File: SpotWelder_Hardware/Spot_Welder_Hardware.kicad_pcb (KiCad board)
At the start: 2 copper layers, 263.7 x 182.9 mm, 158 parts, among them J1 Mini USB, J2 Conn_01x03_Male, Q1 Q_NMOS_GSD, Q10 Q_NMOS_GDS, Q11 Q_NMOS_GDS, Q12 Q_NMOS_GDS, Q13 Q_NMOS_GDS, Q2 MBT3904, Q3 Q_NMOS_GDS, Q4 Q_NMOS_GDS, Q5 Q_NMOS_GDS, Q6 Q_NMOS_GDS, Q7 Q_NMOS_GDS, Q8 Q_NMOS_GDS, Q9 Q_NMOS_GDS, SW1 SW_Push, SW2 SW_SPDT, SW3 Lead Voltage Trigger, SW4 SW_Push, U1 OKI, U2 ATMEGA328P, U3 FAN3122TMXCT-ND, U4 FT232RL, U5 FAN3122TMXCT-ND, Y1 Crystal

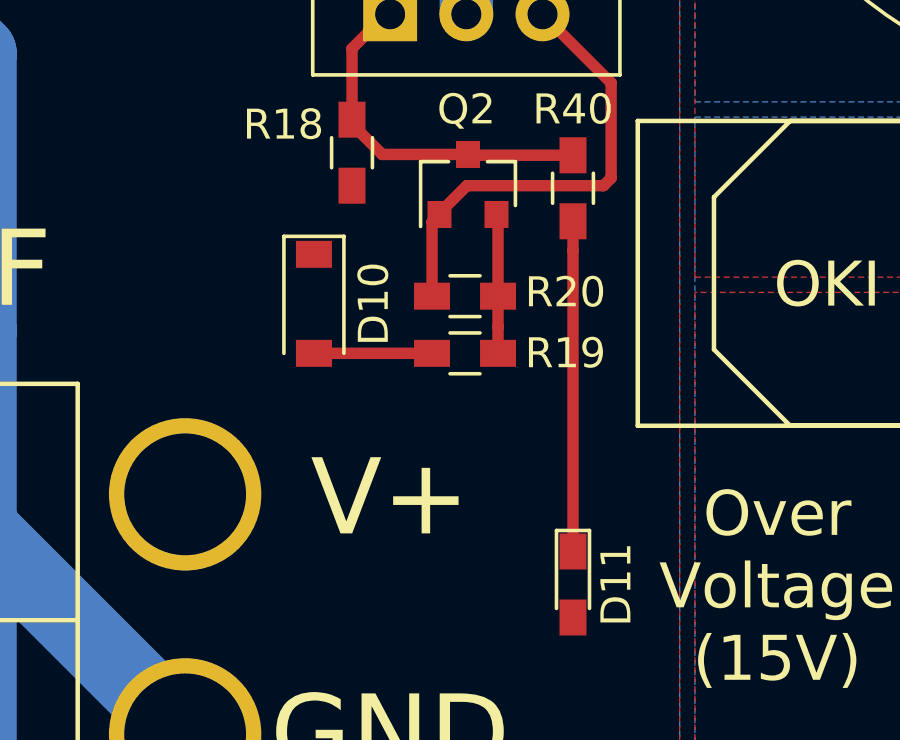
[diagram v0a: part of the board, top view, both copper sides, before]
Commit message: Cleaned repo structure and updated library mappings
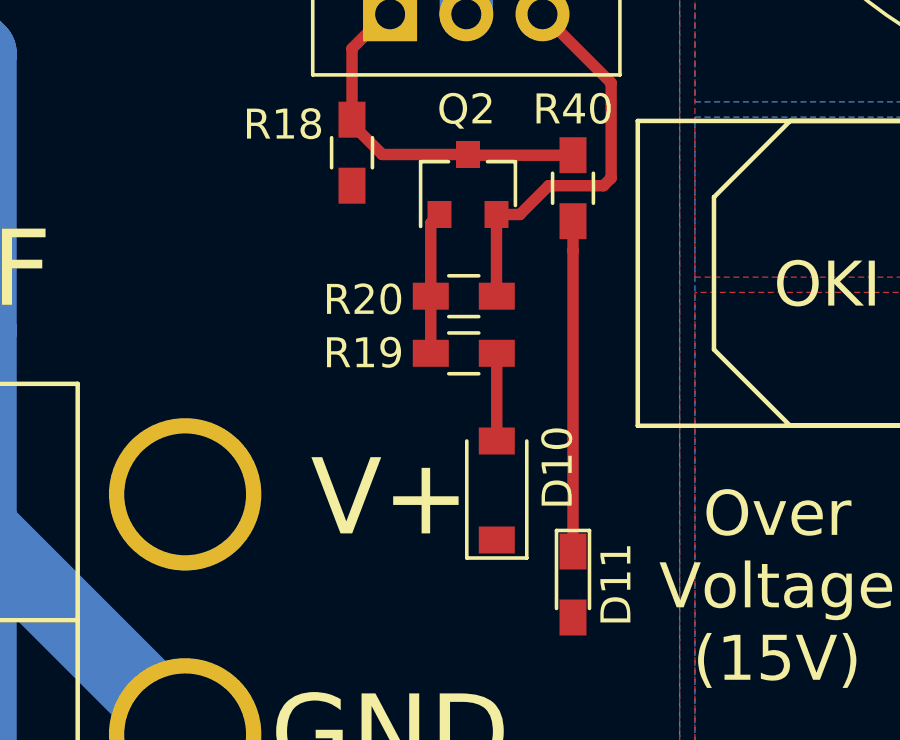
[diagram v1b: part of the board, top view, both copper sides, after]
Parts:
- moved D10 8.71 mm to (47.8, 152.4), turned to 90 degrees
- turned R19 to 0 degrees
- turned R20 to 0 degrees
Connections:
- J1 pad 4: (no net) -> Net-(J1-Pad4)
- Q2 pad 1: Power_GND -> Net-(Q2-Pad1)
- Q2 pad 2: Net-(Q2-Pad2) -> Power_GND
- R19 pad 1: Net-(Q2-Pad2) -> Net-(Q2-Pad1)
- R20 pad 1: Net-(Q2-Pad2) -> Net-(Q2-Pad1)
- U2 pad 14: (no net) -> Net-(U2-Pad14)
- U2 pad 19: (no net) -> Net-(U2-Pad19)
- U2 pad 25: (no net) -> Net-(U2-Pad25)
- U2 pad 26: (no net) -> Net-(U2-Pad26)
- U2 pad 27: (no net) -> Net-(U2-Pad27)
- U2 pad 28: (no net) -> Net-(U2-Pad28)
- U2 pad 4: (no net) -> Net-(U2-Pad4)
- U2 pad 5: (no net) -> Net-(U2-Pad5)
- U4 pad 10: (no net) -> Net-(U4-Pad10)
- U4 pad 11: (no net) -> Net-(U4-Pad11)
- U4 pad 12: (no net) -> Net-(U4-Pad12)
- U4 pad 13: (no net) -> Net-(U4-Pad13)
- U4 pad 14: (no net) -> Net-(U4-Pad14)
- U4 pad 24: (no net) -> Net-(U4-Pad24)
- U4 pad 27: (no net) -> Net-(U4-Pad27)
- U4 pad 28: (no net) -> Net-(U4-Pad28)
- U4 pad 3: (no net) -> Net-(U4-Pad3)
- U4 pad 6: (no net) -> Net-(U4-Pad6)
- U4 pad 8: (no net) -> Net-(U4-Pad8)
- U4 pad 9: (no net) -> Net-(U4-Pad9)
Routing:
- net Net-(Q2-Pad1): track 0.00 -> 4.75 mm
- net Net-(Q2-Pad2): track 4.65 -> 0.00 mm
- net Power_GND: track 15.6 -> 13.5 mm
- net Net-(D10-Pad2): track 4.11 -> 2.92 mm

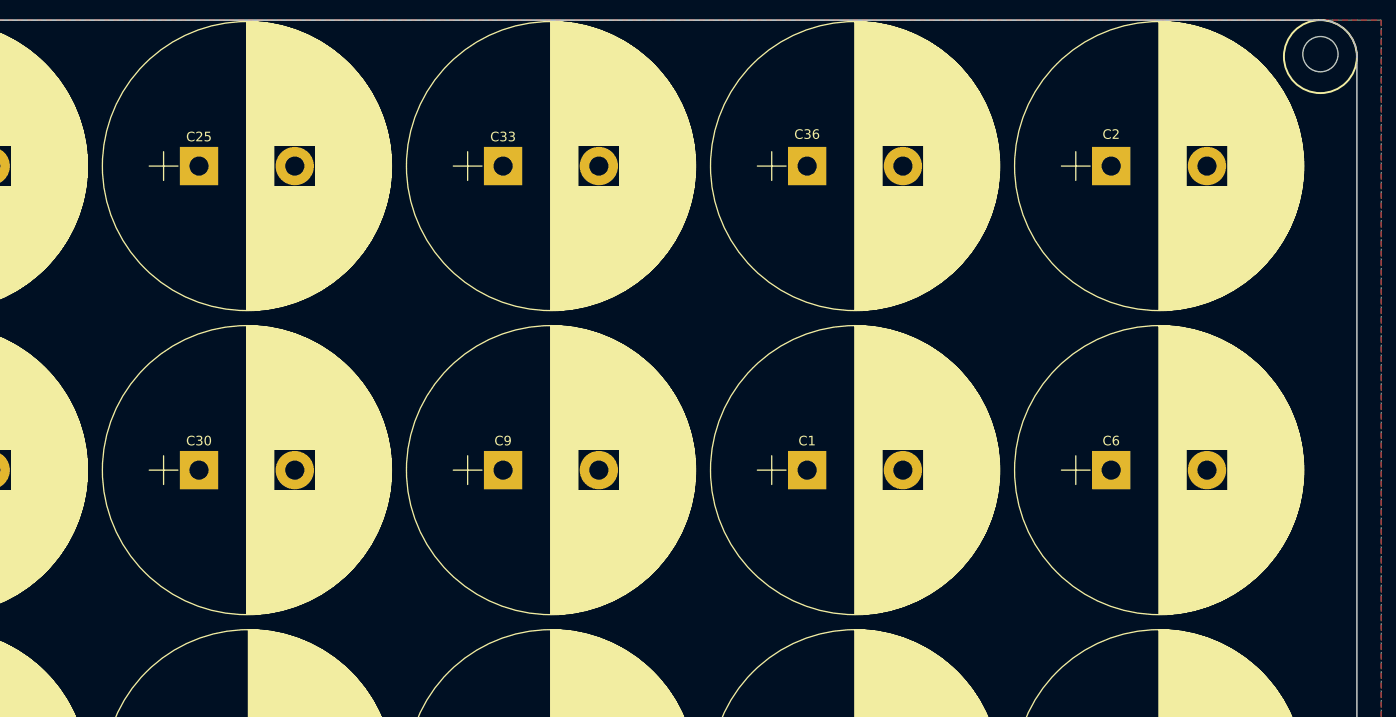
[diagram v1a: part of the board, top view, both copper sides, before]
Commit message: Added center support hole
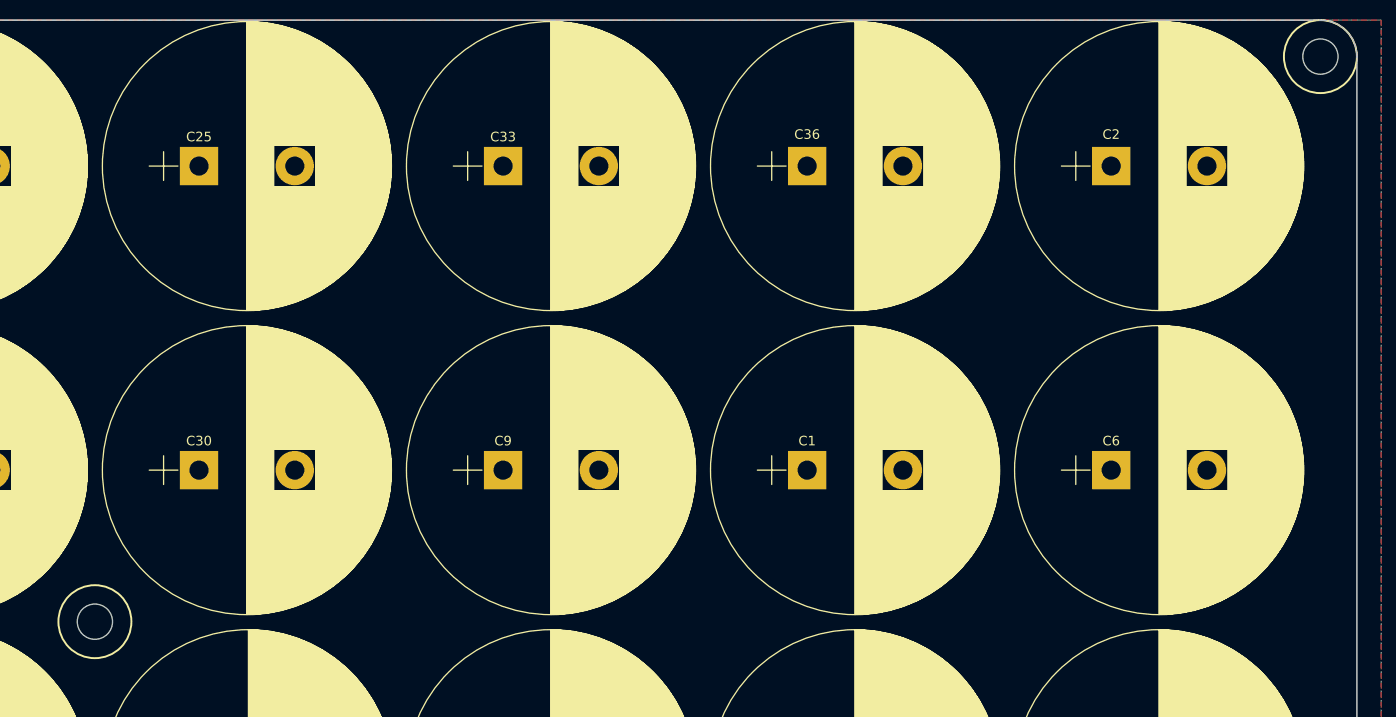
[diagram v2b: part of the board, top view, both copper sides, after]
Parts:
- added REF**: 6-32 Screw Hole, Project Library:6-32 Screw Hole, F.Cu at (139.5, 83.1)
- D10: value 15V -> 14V
- moved REF** 0.25 mm to (276.6, 17.5)
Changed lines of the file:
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@@
   (general
     (thickness 1.6)
-    (drawings 42)
+    (drawings 43)
     (tracks 595)
     (zones 0)
-    (modules 158)
+    (modules 159)
     (nets 95)
   )
@@
   )
   (module "Project Library:6-32 Screw Hole" (layer F.Cu)
+    (at 139.4968 83.1342 90)
+    (fp_text reference REF** (at 0 0.5 90) (layer F.SilkS) hide
+      (effects (font (size 1 1) (thickness 0.15)))
+    )
+    (fp_text value "6-32 Screw Hole" (at 0 -0.5 90) (layer F.Fab)
+      (effects (font (size 1 1) (thickness 0.15)))
+    )
+    (pad "" np_thru_hole circle (at 6.604 9.144 90) (size 3.683 3.683) (drill 3.683) (layers *.Cu *.Mask))
+  )
+  (module "Project Library:6-32 Screw Hole" (layer F.Cu)
     (at 274.574 192.786 180)
     (fp_text reference REF** (at 0 0.5 180) (layer F.SilkS) hide
@@
   )
   (module "Project Library:6-32 Screw Hole" (layer F.Cu)
-    (at 276.606 17.272 270)
+    (at 276.606 17.526 270)
     (fp_text reference REF** (at 0 0.5 270) (layer F.SilkS) hide
       (effects (font (size 1 1) (thickness 0.15)))
@@
       (effects (font (size 1 1) (thickness 0.15)))
     )
-    (fp_text value 15V (at 0 2.1 90) (layer F.Fab)
+    (fp_text value 14V (at 0 2.1 90) (layer F.Fab)
       (effects (font (size 1 1) (thickness 0.15)))
     )
@@
       (xy -6.395956 -0.780515) (xy -6.39578 -0.780671) (xy -6.278558 -0.884008) (xy -6.152213 -0.877709)) (layer F.SilkS) (width 0.01))
   )
+  (gr_circle (center 148.6408 76.5302) (end 152.4508 76.5302) (layer F.SilkS) (width 0.2))
   (gr_circle (center 276.606 192.786) (end 280.416 192.786) (layer F.SilkS) (width 0.2))
   (gr_arc (start 276.606 192.786) (end 276.606 196.596) (angle -90) (layer Edge.Cuts) (width 0.15))

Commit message: Updated version number
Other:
- board text added: "Spot Welder, Rev 3 Mars Rover Design Team, 2020 Missouri S&T Andrew Van Horn With help from Robert Ruark"
- board text removed: "Spot Welder, Rev 2 Mars Rover Design Team, 2019 Missouri S&T Andrew Van Horn With help from Robert Ruark"
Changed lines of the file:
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@@
     (effects (font (size 1.5 1.5) (thickness 0.3)))
   )
-  (gr_text "Spot Welder, Rev 2\nMars Rover Design Team, 2019\nMissouri S&T\nAndrew Van Horn\nWith help from Robert Ruark" (at 232.664 148.59) (layer F.SilkS)
+  (gr_text "Spot Welder, Rev 3\nMars Rover Design Team, 2020\nMissouri S&T\nAndrew Van Horn\nWith help from Robert Ruark" (at 232.664 148.59) (layer F.SilkS)
     (effects (font (size 1.5 1.5) (thickness 0.3)) (justify left))
   )
